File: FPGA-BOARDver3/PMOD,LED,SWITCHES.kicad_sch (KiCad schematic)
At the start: 86 parts, among them P1 PMOD-Device-x2-Type-Generic-A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, P2 PMOD-Device-x2-Type-Generic-A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, Q1 BC107, Q2 BC107, Q3 BC107, Q4 BC107, Q5 BC107, Q6 BC107, SW1 SW_SPDT, SW2 SW_SPDT

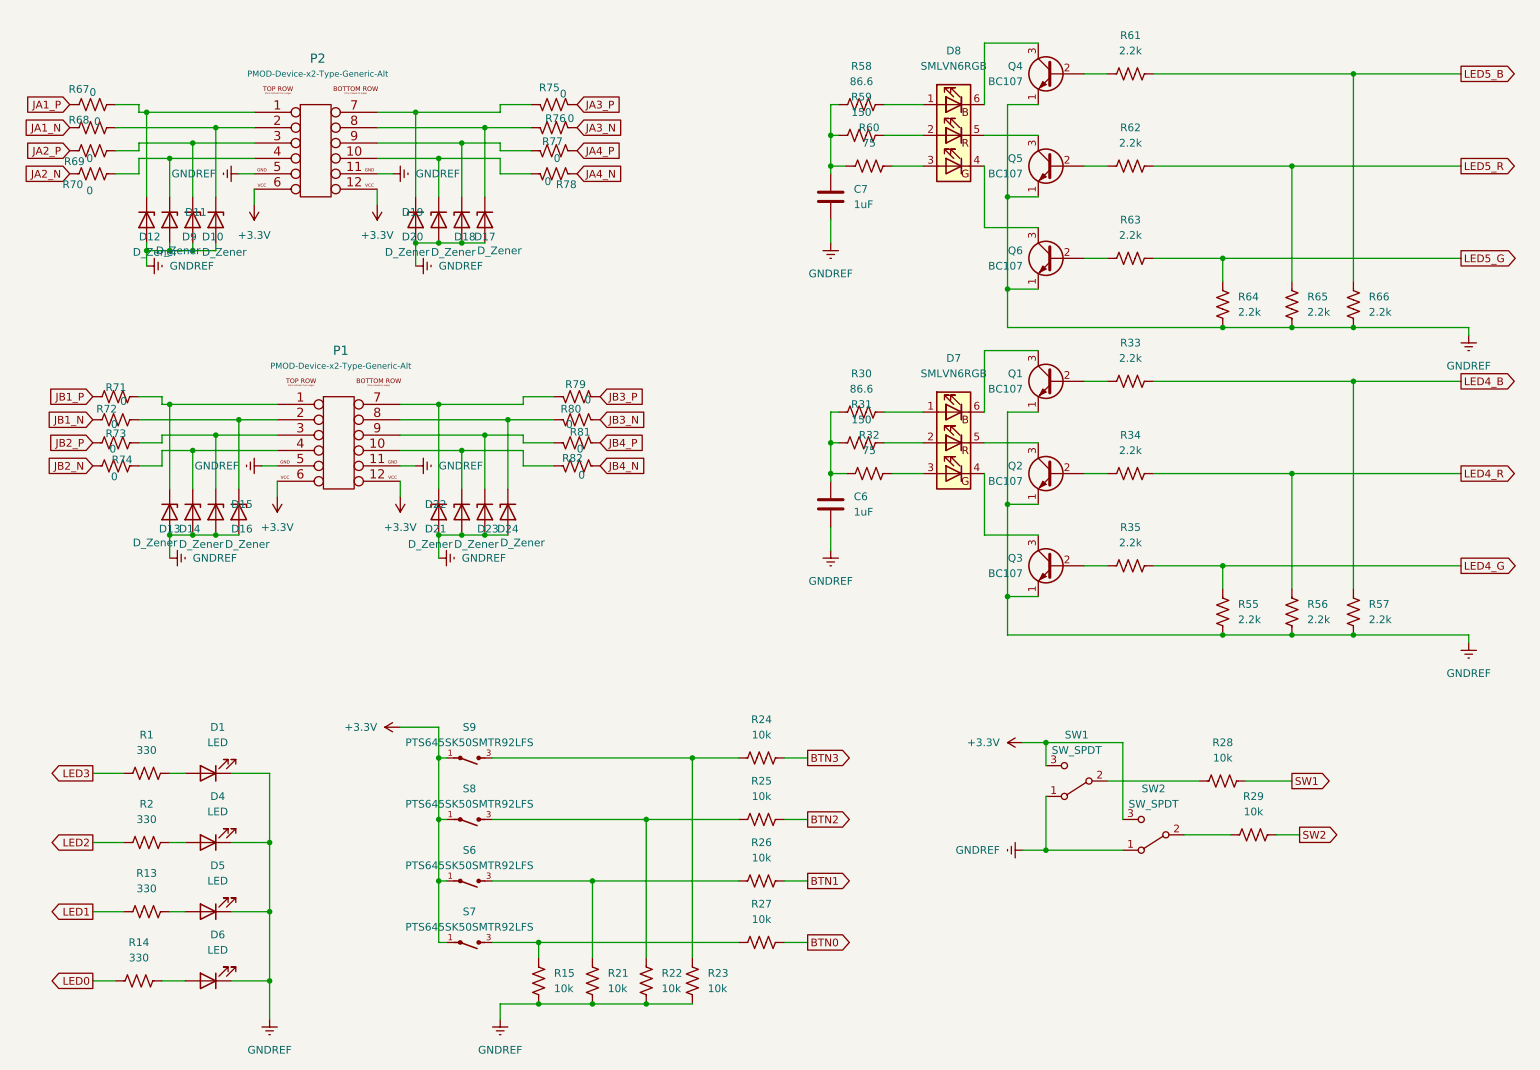
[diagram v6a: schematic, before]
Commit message: added audio out and usb
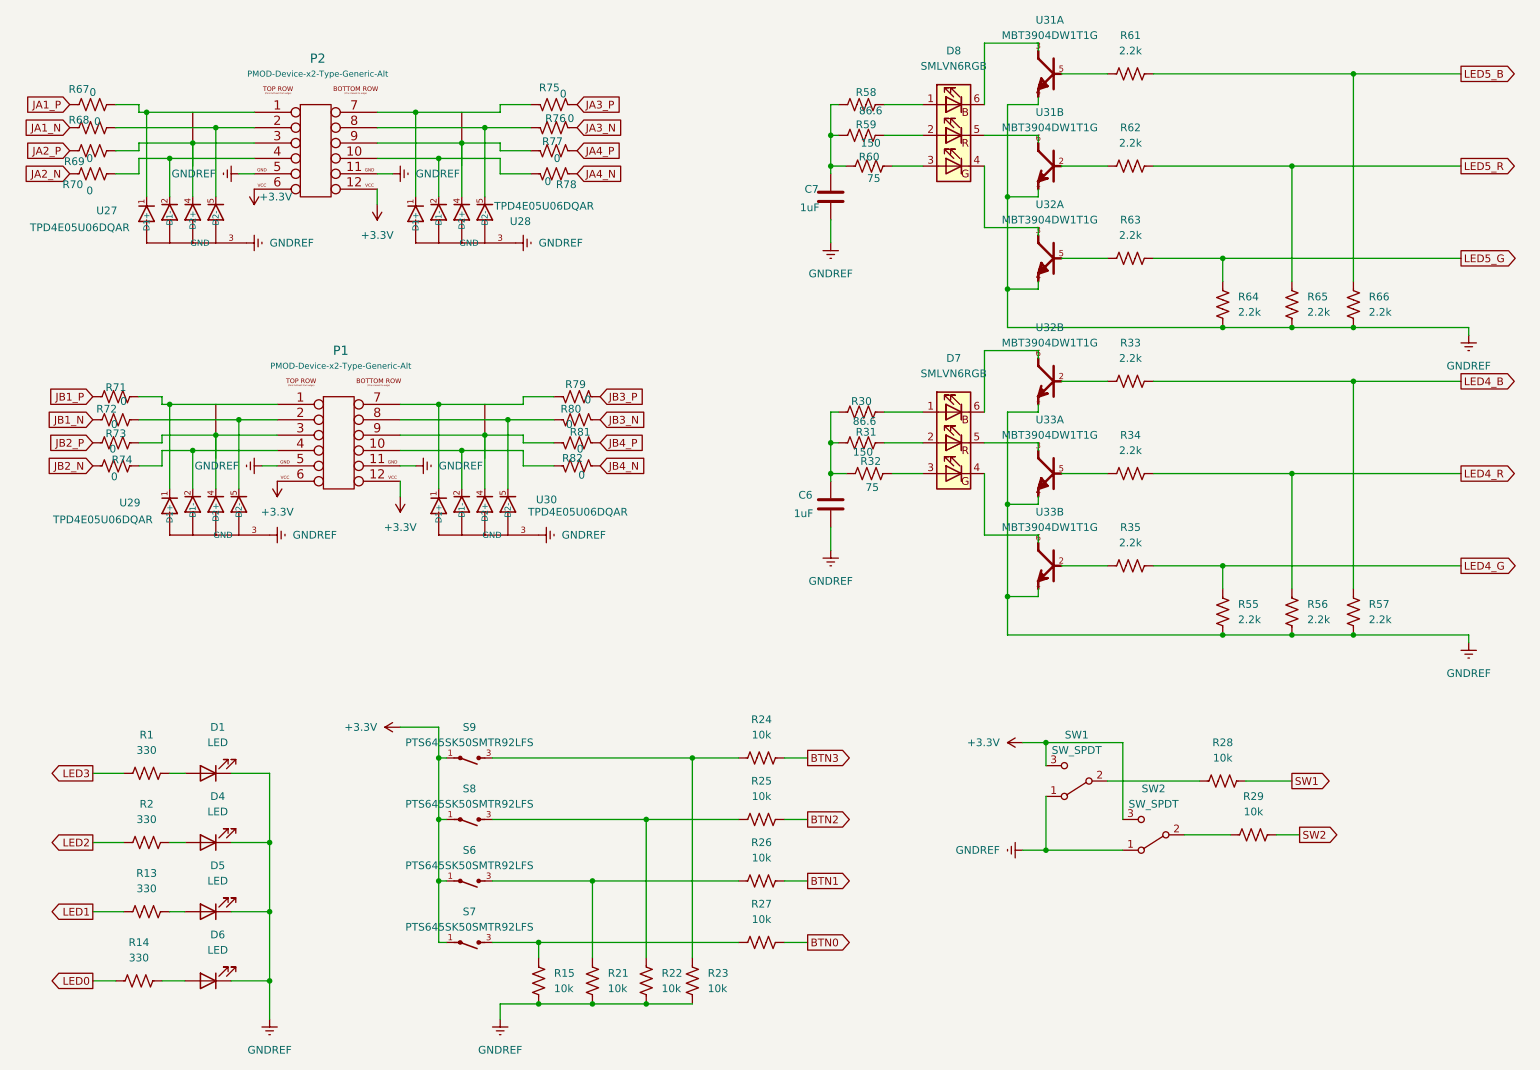
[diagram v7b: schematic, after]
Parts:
- removed D10, D11, D12, D13, D14, D15, D16, D17, D18, D19, D20, D21, D22, D23, D24, D9: D_Zener, footprints:SOD123_DIO, symbol Device:D_Zener
- removed Q1, Q2, Q3, Q4, Q5, Q6: BC107, footprints:TO-18-3, symbol Transistor_BJT:BC107
- added U27, U28, U29, U30: TPD4E05U06DQAR, footprints:IC_TPD4E05U06DQAR, symbol TPD4E05U06DQAR:TPD4E05U06DQAR
- added U31, U32, U33: MBT3904DW1T1G, footprints:SOT236, symbol MBT3904DW1T1G:MBT3904DW1T1G
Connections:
- net GNDREF: now also U27.3 (GND), U28.3 (GND), U29.3 (GND), U30.3 (GND), U31.1, U31.4, U32.1, U32.4, U33.1, U33.4
- net at P2.9 (P9), R77.2: now also U28.4 (D2+)
- net at R63.1: now also U32.5
- net at D8.4 (GK): now also U32.3
- net at P2.1 (P1), R67.2: now also U27.1 (D1+)
- net at P2.10 (P10), R78.2: now also U28.2 (D1-)
- net at P2.2 (P2), R68.2: now also U27.5 (D2-)
- net at P2.3 (P3), R69.2: now also U27.4 (D2+)
- net at P2.4 (P4), R70.2: now also U27.2 (D1-)
- net at P2.7 (P7), R75.2: now also U28.1 (D1+)
- net at P2.8 (P8), R76.2: now also U28.5 (D2-)
- net at P1.9 (P9), R81.2: now also U30.4 (D2+)
- net at P1.1 (P1), R71.2: now also U29.1 (D1+)
- net at D7.4 (GK): now also U33.6
- net at D7.5 (RK): now also U33.3
- net at D7.6 (BK): now also U32.6
- net at R34.1: now also U33.5
- net at R35.1: now also U33.2
- net at P1.10 (P10), R82.2: now also U30.2 (D1-)
- net at P1.2 (P2), R72.2: now also U29.5 (D2-)
- net at P1.3 (P3), R73.2: now also U29.4 (D2+)
- net at P1.4 (P4), R74.2: now also U29.2 (D1-)
- net at P1.7 (P7), R79.2: now also U30.1 (D1+)
- net at P1.8 (P8), R80.2: now also U30.5 (D2-)
- net at R61.1: now also U31.5
- net at R62.1: now also U31.2
- net at D8.5 (RK): now also U31.6
- net at R33.1: now also U32.2
- net at D8.6 (BK): now also U31.3
- new net GND__1: U27.8 (GND__1), U28.8 (GND__1), U29.8 (GND__1), U30.8 (GND__1)

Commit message: updated schematic and layout
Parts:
- C6: value 1uF -> 1uF /10V; LCSC PN (none) -> c14445
- C7: value 1uF -> 1uF / 10V; LCSC PN (none) -> c14445
- D1, D4, D5, D6: LCSC PN (none) -> C434449
- D7, D8: LCSC PN (none) -> C2909770
- R1, R13, R14, R2: LCSC PN (none) -> C105875
- R15, R21, R22, R23, R24, R25, R26, R27, R28, R29: LCSC PN (none) -> C60490
- R30, R58: LCSC PN (none) -> C295882
- R31, R59: LCSC PN (none) -> C138054
- R32, R60: LCSC PN (none) -> C114757
- R33, R34, R35, R55, R56, R57, R61, R62, R63, R64, R65, R66: LCSC PN (none) -> c114762
- R67, R68, R69, R70, R71, R72, R73, R74, R75, R76, R77, R78, R79, R80, R81, R82: LCSC PN (none) -> C106231
- S6, S7, S8, S9: LCSC PN (none) -> C221872
- SW0: renamed from SW2; footprint footprints:SS-12D10G5_XKB -> footprints:SW_EG1218
- SW1: footprint footprints:SS-12D10G5_XKB -> footprints:SW_EG1218
- U27, U28, U29, U30: LCSC PN (none) -> C138714
- U31, U32, U33: LCSC PN (none) -> C110150
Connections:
- net GND__1: no longer U29.8 (GND__1)
- net at P2.10 (P10), R78.2: now also U28.5 (D2-); no longer U28.2 (D1-)
- net at P2.2 (P2), R68.2: now also U27.2 (D1-); no longer U27.5 (D2-)
- net at P2.4 (P4), R70.2: now also U27.5 (D2-); no longer U27.2 (D1-)
- net at P2.8 (P8), R76.2: now also U28.2 (D1-); no longer U28.5 (D2-)
- net +5V: now reaches C7.1, R58.1, R59.1, R60.1
- net +5V: now also C6.1, R30.1, R31.1, R32.1
- net at P1.1 (P1), R71.2: now also U29.5 (D2-); no longer U29.1 (D1+)
- net at P1.2 (P2), R72.2: now also U29.4 (D2+); no longer U29.5 (D2-)
- net at P1.3 (P3), R73.2: now also U29.1 (D1+); no longer U29.4 (D2+)
- net at P1.7 (P7), R79.2: now also U30.4 (D2+); no longer U30.1 (D1+)
- net at P1.9 (P9), R81.2: now also U30.1 (D1+); no longer U30.4 (D2+)
- net +3.3V renamed +3V3
- net SW2 renamed SW0
